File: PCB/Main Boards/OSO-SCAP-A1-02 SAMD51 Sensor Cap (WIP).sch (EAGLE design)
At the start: 68 parts, among them J1 10118193-0001LF, J2 S2B-PH-SM4-TB(LF)(SN), J3 S3B-PH-SM4-TB(LF)(SN), J4 SM04B-SRSS-TB(LF)(SN), Q1 DMG341, SW1 SPST_TACT-KMR2, SW2 SPST_TACT-KMR2, U1 AP2112-3.3, U2 MCP73831T-2ACI/OT, U3 ATSAMD51G18A-MUT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

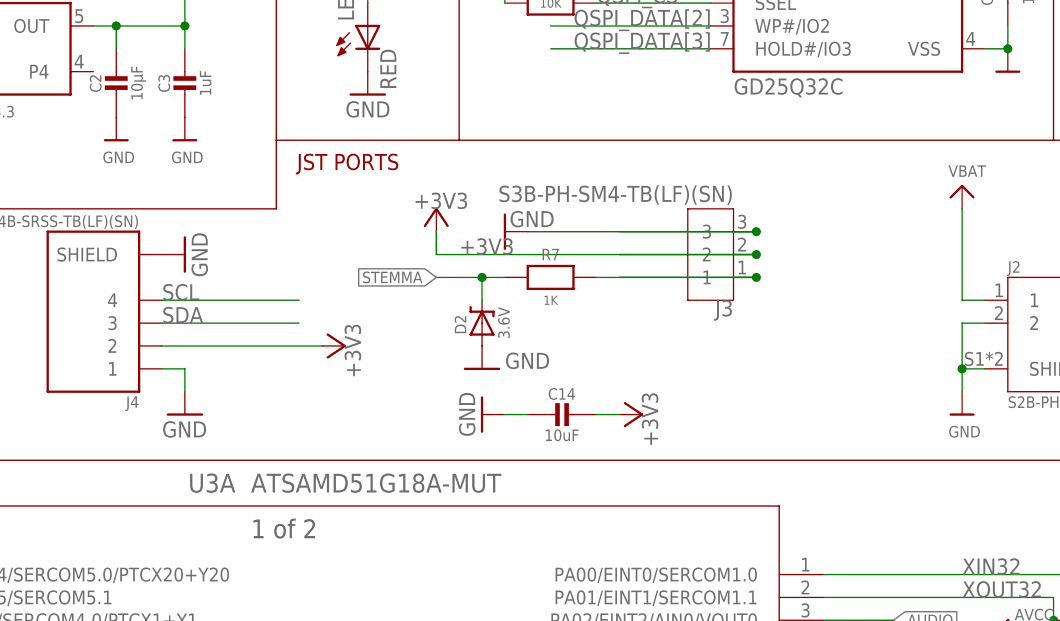
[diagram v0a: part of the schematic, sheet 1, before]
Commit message: A1 rev 02: add i2c pull-ups
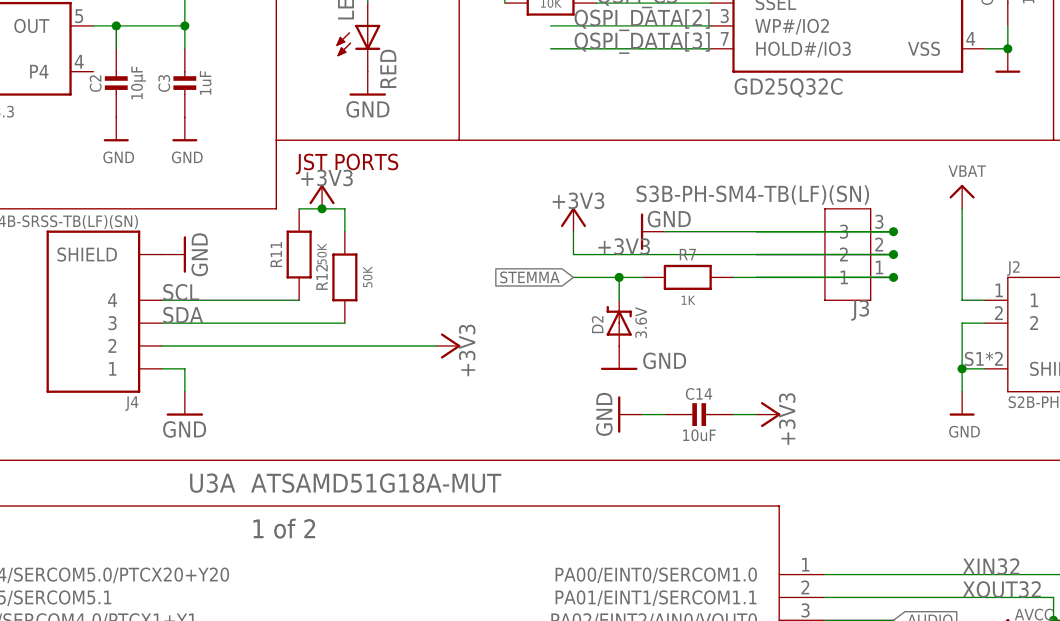
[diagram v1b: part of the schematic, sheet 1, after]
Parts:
- added R11, R12: 50K, microbuilder:RESISTOR0805_NOOUTLINE
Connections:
- net +3V3: now also R11.2, R12.2
- net SCL: now also R11.1
- net SDA: now also R12.1
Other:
- moved on the sheet: C14, D2, J3, R7

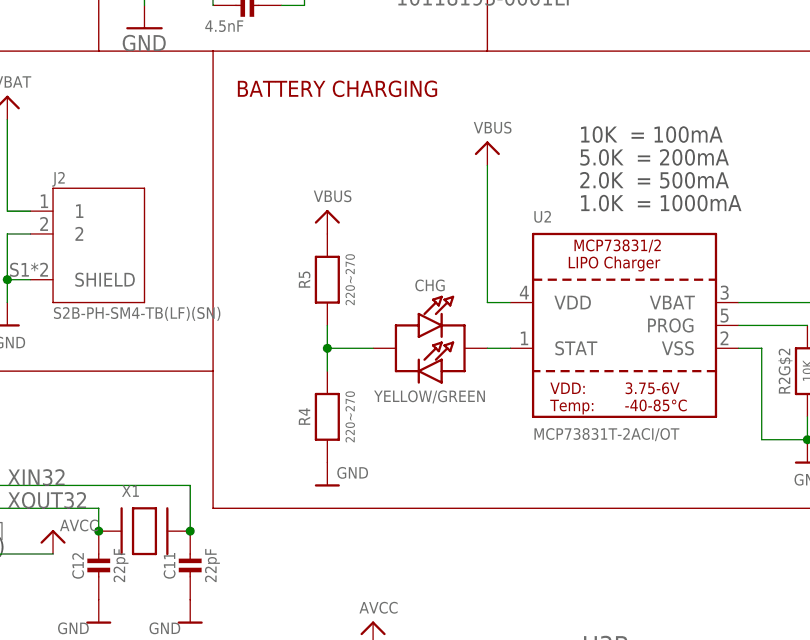
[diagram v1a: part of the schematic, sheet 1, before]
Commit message: CHG and FUL now separate LEDs
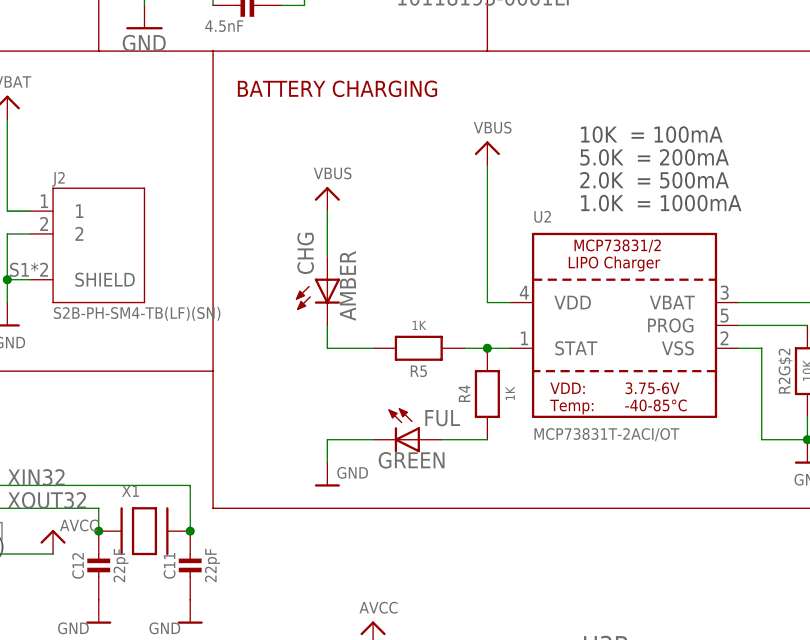
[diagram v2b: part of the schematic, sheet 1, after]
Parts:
- added FUL: GREEN, adafruit:LEDCHIPLED_0603
- CHG: value YELLOW/GREEN -> AMBER; device My Stuff:LED_BIDI1206 -> adafruit:LEDCHIPLED_0603
- LED: device adafruit:LEDCHIPLED_1206 -> adafruit:LEDCHIPLED_0805
- R4, R5: value 220~270 -> 1K
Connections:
- removed net N$1: CHG.A, R4.2, R5.1
- new net N$6: CHG.C, R5.2
- new net N$7: FUL.A, R4.1
- net GND: now also FUL.C; no longer R4.1
- net STAT: now also R4.2, R5.1; no longer CHG.C
- net VBUS: now also CHG.A; no longer R5.2
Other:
- moved on the sheet: R4, R5
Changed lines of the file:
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@@
 </variantdefs>
 <classes>
-<class number="0" name="default" width="0.1524" drill="0.254">
+<class number="0" name="default" width="0" drill="0">
 </class>
 <class number="1" name="power" width="0.3048" drill="0.3048">
@@
 <part name="U$21" library="microbuilder" deviceset="GND" device=""/>
 <part name="U2" library="microbuilder" deviceset="MCP73831/2" device="" value="MCP73831T-2ACI/OT"/>
-<part name="R5" library="microbuilder" deviceset="RESISTOR" device="0805_NOOUTLINE" value="220~270"/>
+<part name="R5" library="microbuilder" deviceset="RESISTOR" device="0805_NOOUTLINE" value="1K"/>
 <part name="C4" library="microbuilder" deviceset="CAP_CERAMIC" device="0805-NOOUTLINE" value="10µF"/>
 <part name="U$33" library="microbuilder" deviceset="GND" device=""/>
@@
 <part name="TP2" library="microbuilder" deviceset="TESTPOINT" device="ROUND1.5MMNO"/>
 <part name="TP3" library="microbuilder" deviceset="TESTPOINT" device="ROUND1.5MMNO"/>
-<part name="LED" library="adafruit" deviceset="LED" device="CHIPLED_1206" value="RED"/>
+<part name="LED" library="adafruit" deviceset="LED" device="CHIPLED_0805" value="RED"/>
 <part name="P+1" library="supply1" library_urn="urn:adsk.eagle:library:371" deviceset="V+" device=""/>
-<part name="R4" library="microbuilder" deviceset="RESISTOR" device="0805_NOOUTLINE" value="220~270"/>
+<part name="R4" library="microbuilder" deviceset="RESISTOR" device="0805_NOOUTLINE" value="1K"/>
 <part name="J4" library="SM04B-SRSS-TB_LF__SN_" deviceset="SM04B-SRSS-TB(LF)(SN)" device=""/>
 <part name="+3V5" library="supply1" library_urn="urn:adsk.eagle:library:371" deviceset="+3V3" device=""/>
@@
 <part name="GND11" library="supply1" deviceset="GND" device=""/>
 <part name="+3V10" library="supply1" library_urn="urn:adsk.eagle:library:371" deviceset="+3V3" device=""/>
-<part name="CHG" library="My Stuff" deviceset="LED_BIDI" device="1206" value="YELLOW/GREEN"/>
 <part name="U$15" library="microbuilder" deviceset="VBUS" device=""/>
 <part name="U$18" library="microbuilder" deviceset="GND" device=""/>
@@
 <part name="R12" library="microbuilder" deviceset="RESISTOR" device="0805_NOOUTLINE" value="50K"/>
 <part name="+3V17" library="supply1" library_urn="urn:adsk.eagle:library:371" deviceset="+3V3" device=""/>
+<part name="CHG" library="adafruit" deviceset="LED" device="CHIPLED_0603" value="AMBER"/>
+<part name="FUL" library="adafruit" deviceset="LED" device="CHIPLED_0603" value="GREEN"/>
 </parts>
 <sheets>
@@
 <attribute name="VALUE" x="213.36" y="96.52" size="1.27" layer="95"/>
 </instance>
-<instance part="R5" gate="G$1" x="190.5" y="114.3" smashed="yes" rot="R90">
-<attribute name="NAME" x="187.96" y="114.3" size="1.27" layer="95" font="vector" rot="R90" align="center"/>
-<attribute name="VALUE" x="193.04" y="114.3" size="1.016" layer="96" font="vector" ratio="15" rot="R90" align="center"/>
+<instance part="R5" gate="G$1" x="200.66" y="106.68" smashed="yes" rot="R180">
+<attribute name="NAME" x="200.66" y="104.14" size="1.27" layer="95" font="vector" rot="R180" align="center"/>
+<attribute name="VALUE" x="200.66" y="109.22" size="1.016" layer="96" font="vector" ratio="15" rot="R180" align="center"/>
 </instance>
 <instance part="C4" gate="G$1" x="251.46" y="104.14" smashed="yes">
@@
 <attribute name="VALUE" x="30.48" y="157.48" size="1.778" layer="96" rot="R180"/>
 </instance>
-<instance part="R4" gate="G$1" x="190.5" y="99.06" smashed="yes" rot="R90">
-<attribute name="NAME" x="187.96" y="99.06" size="1.27" layer="95" font="vector" rot="R90" align="center"/>
-<attribute name="VALUE" x="193.04" y="99.06" size="1.016" layer="96" font="vector" ratio="15" rot="R90" align="center"/>
+<instance part="R4" gate="G$1" x="208.28" y="101.6" smashed="yes" rot="R90">
+<attribute name="NAME" x="205.74" y="101.6" size="1.27" layer="95" font="vector" rot="R90" align="center"/>
+<attribute name="VALUE" x="210.82" y="101.6" size="1.016" layer="96" font="vector" ratio="15" rot="R90" align="center"/>
 </instance>
 <instance part="+3V5" gate="G$1" x="195.58" y="59.69" smashed="yes" rot="MR0">
@@
 <attribute name="VALUE" x="55.88" y="340.36" size="1.016" layer="96" font="vector" ratio="15" rot="R270" align="center"/>
 </instance>
-<instance part="CHG" gate="G$1" x="203.2" y="106.68" smashed="yes">
-<attribute name="NAME" x="201.93" y="113.665" size="1.27" layer="95" align="center"/>
-<attribute name="VALUE" x="201.93" y="101.346" size="1.27" layer="96" align="center"/>
-</instance>
-<instance part="U$15" gate="G$1" x="190.5" y="121.92" smashed="yes">
-<attribute name="VALUE" x="188.976" y="122.936" size="1.27" layer="96"/>
+<instance part="U$15" gate="G$1" x="190.5" y="124.46" smashed="yes">
+<attribute name="VALUE" x="188.976" y="125.476" size="1.27" layer="96"/>
 </instance>
 <instance part="U$18" gate="G$1" x="190.5" y="91.44" smashed="yes">
@@
 <instance part="+3V17" gate="G$1" x="83.82" y="134.62" smashed="yes">
 <attribute name="VALUE" x="81.28" y="134.62" size="1.778" layer="96"/>
+</instance>
+<instance part="CHG" gate="G$1" x="190.5" y="114.3" smashed="yes">
+<attribute name="NAME" x="188.976" y="114.808" size="1.778" layer="95" rot="R90"/>
+<attribute name="VALUE" x="193.675" y="109.728" size="1.778" layer="96" rot="R90"/>
+</instance>
+<instance part="FUL" gate="G$1" x="200.66" y="96.52" smashed="yes" rot="R270">
+<attribute name="NAME" x="201.168" y="98.044" size="1.778" layer="95"/>
+<attribute name="VALUE" x="196.088" y="93.345" size="1.778" layer="96"/>
 </instance>
 </instances>
@@
 </segment>
 <segment>
-<pinref part="U$18" gate="G$1" pin="GND"/>
-<pinref part="R4" gate="G$1" pin="1"/>
-</segment>
-<segment>
 <pinref part="U$21" gate="G$1" pin="GND"/>
 <pinref part="R1" gate="G$1" pin="1"/>
@@
 <pinref part="J4" gate="G$2" pin="SHIELD"/>
 <pinref part="GND12" gate="1" pin="GND"/>
+</segment>
+<segment>
+<pinref part="FUL" gate="G$1" pin="C"/>
+<pinref part="U$18" gate="G$1" pin="GND"/>
+<wire x1="195.58" y1="96.52" x2="190.5" y2="96.52" width="0.1524" layer="91"/>
+<wire x1="190.5" y1="96.52" x2="190.5" y2="93.98" width="0.1524" layer="91"/>
 </segment>
 </net>
@@
 </segment>
 <segment>
+<pinref part="CHG" gate="G$1" pin="A"/>
 <pinref part="U$15" gate="G$1" pin="VBUS"/>
-<pinref part="R5" gate="G$1" pin="2"/>
+<wire x1="190.5" y1="116.84" x2="190.5" y2="121.92" width="0.1524" layer="91"/>
 </segment>
 </net>
@@
 </segment>
 </net>
-<net name="N$1" class="0">
-<segment>
+<net name="STAT" class="0">
+<segment>
+<pinref part="U2" gate="G$1" pin="STAT"/>
+<wire x1="208.28" y1="106.68" x2="210.82" y2="106.68" width="0.1524" layer="91"/>
+<pinref part="R4" gate="G$1" pin="2"/>
 <pinref part="R5" gate="G$1" pin="1"/>
-<pinref part="R4" gate="G$1" pin="2"/>
-<wire x1="190.5" y1="109.22" x2="190.5" y2="106.68" width="0.1524" layer="91"/>
-<pinref part="CHG" gate="G$1" pin="A"/>
-<wire x1="190.5" y1="106.68" x2="190.5" y2="104.14" width="0.1524" layer="91"/>
-<wire x1="195.58" y1="106.68" x2="190.5" y2="106.68" width="0.1524" layer="91"/>
-<junction x="190.5" y="106.68"/>
-</segment>
-</net>
-<net name="STAT" class="0">
-<segment>
-<pinref part="U2" gate="G$1" pin="STAT"/>
-<pinref part="CHG" gate="G$1" pin="C"/>
-<wire x1="208.28" y1="106.68" x2="210.82" y2="106.68" width="0.1524" layer="91"/>
+<wire x1="205.74" y1="106.68" x2="208.28" y2="106.68" width="0.1524" layer="91"/>
+<junction x="208.28" y="106.68"/>
 </segment>
 </net>
@@
 </segment>
 </net>
+<net name="N$6" class="0">
+<segment>
+<pinref part="CHG" gate="G$1" pin="C"/>
+<pinref part="R5" gate="G$1" pin="2"/>
+<wire x1="190.5" y1="109.22" x2="190.5" y2="106.68" width="0.1524" layer="91"/>
+<wire x1="190.5" y1="106.68" x2="195.58" y2="106.68" width="0.1524" layer="91"/>
+</segment>
+</net>
+<net name="N$7" class="0">
+<segment>
+<pinref part="R4" gate="G$1" pin="1"/>
+<pinref part="FUL" gate="G$1" pin="A"/>
+<wire x1="208.28" y1="96.52" x2="203.2" y2="96.52" width="0.1524" layer="91"/>
+</segment>
+</net>
